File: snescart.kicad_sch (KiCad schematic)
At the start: 5 parts, among them P1 CASSETTE, U2 27C512

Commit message: fix cic
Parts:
- removed U1: ~, Package_DIP:DIP-18_W7.62mm, symbol SNES_Library:CIC
- added C3: C, Capacitor_THT:C_Disc_D4.3mm_W1.9mm_P5.00mm, symbol Device:C
- added U2: ~, Package_DIP:DIP-16_W7.62mm, symbol SNES_Library:CARTCIC
- renumbered U2 to U1
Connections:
- net GND: now also U2.4 (GND), U2.8 (GND)
- net VCC: now also U2.16 (Vcc)
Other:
- moved on the sheet: C2
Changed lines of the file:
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@@
 (kicad_sch (version 20230121) (generator eeschema)
   (paper "A4")
-  (junction (at 79.375 53.34) (diameter 0) (color 0 0 0 0)
+  (junction (at 53.34 70.485) (diameter 0) (color 0 0 0 0)
   )
   (junction (at 48.26 98.425) (diameter 0) (color 0 0 0 0)
@@
     (stroke (width 0) (type default))
   )
-  (wire (pts (xy 74.295 53.34) (xy 79.375 53.34))
-    (stroke (width 0) (type default))
-  )
   (wire (pts (xy 48.26 98.425) (xy 69.85 98.425))
     (stroke (width 0) (type default))
@@
     (stroke (width 0) (type default))
   )
-  (wire (pts (xy 79.375 53.34) (xy 85.09 53.34))
-    (stroke (width 0) (type default))
-  )
   (wire (pts (xy 80.01 121.285) (xy 113.03 121.285))
     (stroke (width 0) (type default))
@@
     (stroke (width 0) (type default))
   )
-  (symbol (lib_id "power:GND") (at 85.09 60.96 0) (unit 1)
-    (in_bom yes) (on_board yes) (dnp no) (fields_autoplaced)
-    (property "Reference" "#PWR06" (at 85.09 67.31 0)
-      (effects (font (size 1.27 1.27)) hide)
-    )
-    (property "Value" "GND" (at 85.09 66.04 0)
-      (effects (font (size 1.27 1.27)))
-    )
-    (property "Footprint" "" (at 85.09 60.96 0)
-      (effects (font (size 1.27 1.27)) hide)
-    )
-    (property "Datasheet" "" (at 85.09 60.96 0)
+  (symbol (lib_id "power:GND") (at 53.34 78.105 0) (unit 1)
+    (in_bom yes) (on_board yes) (dnp no) (fields_autoplaced)
+    (property "Reference" "#PWR06" (at 53.34 84.455 0)
+      (effects (font (size 1.27 1.27)) hide)
+    )
+    (property "Value" "GND" (at 53.34 83.185 0)
+      (effects (font (size 1.27 1.27)))
+    )
+    (property "Footprint" "" (at 53.34 78.105 0)
+      (effects (font (size 1.27 1.27)) hide)
+    )
+    (property "Datasheet" "" (at 53.34 78.105 0)
       (effects (font (size 1.27 1.27)) hide)
     )
@@
     )
   )
-  (symbol (lib_id "power:VCC") (at 79.375 53.34 0) (unit 1)
-    (in_bom yes) (on_board yes) (dnp no) (fields_autoplaced)
-    (property "Reference" "#PWR05" (at 79.375 57.15 0)
-      (effects (font (size 1.27 1.27)) hide)
-    )
-    (property "Value" "VCC" (at 79.375 49.53 0)
-      (effects (font (size 1.27 1.27)))
-    )
-    (property "Footprint" "" (at 79.375 53.34 0)
-      (effects (font (size 1.27 1.27)) hide)
-    )
-    (property "Datasheet" "" (at 79.375 53.34 0)
+  (symbol (lib_id "Device:C") (at 43.815 53.975 0) (unit 1)
+    (in_bom yes) (on_board yes) (dnp no) (fields_autoplaced)
+    (property "Reference" "C3" (at 46.99 53.34 0)
+      (effects (font (size 1.27 1.27)) (justify left))
+    )
+    (property "Value" "C" (at 46.99 55.88 0)
+      (effects (font (size 1.27 1.27)) (justify left))
+    )
+    (property "Footprint" "Capacitor_THT:C_Disc_D4.3mm_W1.9mm_P5.00mm" (at 44.7802 57.785 0)
+      (effects (font (size 1.27 1.27)) hide)
+    )
+    (property "Datasheet" "~" (at 43.815 53.975 0)
+      (effects (font (size 1.27 1.27)) hide)
+    )
+    (pin "1")
+    (pin "2")
+    (instances
+      (project "snescart"
+        (path "/066a4729-7396-4945-b543-8e17bff58a3f"
+          (reference "C3") (unit 1)
+        )
+      )
+    )
+  )
+  (symbol (lib_id "power:VCC") (at 53.34 70.485 90) (unit 1)
+    (in_bom yes) (on_board yes) (dnp no)
+    (property "Reference" "#PWR05" (at 57.15 70.485 0)
+      (effects (font (size 1.27 1.27)) hide)
+    )
+    (property "Value" "VCC" (at 46.355 70.485 90)
+      (effects (font (size 1.27 1.27)) (justify right))
+    )
+    (property "Footprint" "" (at 53.34 70.485 0)
+      (effects (font (size 1.27 1.27)) hide)
+    )
+    (property "Datasheet" "" (at 53.34 70.485 0)
       (effects (font (size 1.27 1.27)) hide)
     )
@@
     )
   )
-  (symbol (lib_id "Device:C") (at 85.09 57.15 0) (unit 1)
-    (in_bom yes) (on_board yes) (dnp no) (fields_autoplaced)
-    (property "Reference" "C2" (at 88.9 56.515 0)
+  (symbol (lib_id "Device:C") (at 53.34 74.295 0) (unit 1)
+    (in_bom yes) (on_board yes) (dnp no) (fields_autoplaced)
+    (property "Reference" "C2" (at 57.15 73.66 0)
       (effects (font (size 1.27 1.27)) (justify left))
     )
-    (property "Value" "C" (at 88.9 59.055 0)
+    (property "Value" "C" (at 57.15 76.2 0)
       (effects (font (size 1.27 1.27)) (justify left))
     )
-    (property "Footprint" "Capacitor_THT:C_Disc_D4.3mm_W1.9mm_P5.00mm" (at 86.0552 60.96 0)
-      (effects (font (size 1.27 1.27)) hide)
-    )
-    (property "Datasheet" "~" (at 85.09 57.15 0)
+    (property "Footprint" "Capacitor_THT:C_Disc_D4.3mm_W1.9mm_P5.00mm" (at 54.3052 78.105 0)
+      (effects (font (size 1.27 1.27)) hide)
+    )
+    (property "Datasheet" "~" (at 53.34 74.295 0)
       (effects (font (size 1.27 1.27)) hide)
     )
@@
   (symbol (lib_id "Memory_EPROM:27C512") (at 69.85 126.365 0) (mirror y) (unit 1)
     (in_bom yes) (on_board yes) (dnp no) (fields_autoplaced)
-    (property "Reference" "U2" (at 70.4341 96.52 0)
+    (property "Reference" "U1" (at 70.4341 96.52 0)
       (effects (font (size 1.27 1.27)) (justify right))
     )
@@
       (project "snescart"
         (path "/066a4729-7396-4945-b543-8e17bff58a3f"
-          (reference "U2") (unit 1)
+          (reference "U1") (unit 1)
         )
       )
@@
     )
   )
+  (symbol (lib_id "power:GND") (at 53.34 65.405 270) (unit 1)
+    (in_bom yes) (on_board yes) (dnp no)
+    (property "Reference" "#PWR09" (at 46.99 65.405 0)
+      (effects (font (size 1.27 1.27)) hide)
+    )
+    (property "Value" "GND" (at 46.355 65.405 90)
+      (effects (font (size 1.27 1.27)) (justify left))
+    )
+    (property "Footprint" "" (at 53.34 65.405 0)
+      (effects (font (size 1.27 1.27)) hide)
+    )
+    (property "Datasheet" "" (at 53.34 65.405 0)
+      (effects (font (size 1.27 1.27)) hide)
+    )
+    (pin "1")
+    (instances
+      (project "snescart"
+        (path "/066a4729-7396-4945-b543-8e17bff58a3f"
+          (reference "#PWR09") (unit 1)
+        )
+      )
+    )
+  )
   (symbol (lib_id "power:GND") (at 138.43 133.985 90) (unit 1)
     (in_bom yes) (on_board yes) (dnp no) (fields_autoplaced)
@@
         (path "/066a4729-7396-4945-b543-8e17bff58a3f"
           (reference "#PWR08") (unit 1)
-        )
-      )
-    )
-  )
-  (symbol (lib_id "SNES_Library:CIC") (at 66.675 62.23 0) (unit 1)
-    (in_bom yes) (on_board yes) (dnp no) (fields_autoplaced)
-    (property "Reference" "U1" (at 66.04 50.165 0)
-      (effects (font (size 1.27 1.27)))
-    )
-    (property "Value" "~" (at 61.595 48.26 0)
-      (effects (font (size 1.27 1.27)))
-    )
-    (property "Footprint" "Package_DIP:DIP-18_W7.62mm" (at 61.595 48.26 0)
-      (effects (font (size 1.27 1.27)) hide)
-    )
-    (property "Datasheet" "" (at 61.595 48.26 0)
-      (effects (font (size 1.27 1.27)) hide)
-    )
-    (pin "1")
-    (pin "10")
-    (pin "11")
-    (pin "12")
-    (pin "13")
-    (pin "14")
-    (pin "15")
-    (pin "16")
-    (pin "17")
-    (pin "18")
-    (pin "2")
-    (pin "3")
-    (pin "4")
-    (pin "5")
-    (pin "6")
-    (pin "7")
-    (pin "8")
-    (pin "9")
-    (instances
-      (project "snescart"
-        (path "/066a4729-7396-4945-b543-8e17bff58a3f"
-          (reference "U1") (unit 1)
         )
       )
@@
     )
   )
-  (symbol (lib_id "power:GND") (at 57.785 73.66 0) (unit 1)
-    (in_bom yes) (on_board yes) (dnp no) (fields_autoplaced)
-    (property "Reference" "#PWR04" (at 57.785 80.01 0)
-      (effects (font (size 1.27 1.27)) hide)
-    )
-    (property "Value" "GND" (at 57.785 78.74 0)
-      (effects (font (size 1.27 1.27)))
-    )
-    (property "Footprint" "" (at 57.785 73.66 0)
-      (effects (font (size 1.27 1.27)) hide)
-    )
-    (property "Datasheet" "" (at 57.785 73.66 0)
+  (symbol (lib_id "power:GND") (at 53.34 67.945 270) (unit 1)
+    (in_bom yes) (on_board yes) (dnp no)
+    (property "Reference" "#PWR04" (at 46.99 67.945 0)
+      (effects (font (size 1.27 1.27)) hide)
+    )
+    (property "Value" "GND" (at 46.355 67.945 90)
+      (effects (font (size 1.27 1.27)) (justify left))
+    )
+    (property "Footprint" "" (at 53.34 67.945 0)
+      (effects (font (size 1.27 1.27)) hide)
+    )
+    (property "Datasheet" "" (at 53.34 67.945 0)
       (effects (font (size 1.27 1.27)) hide)
     )
@@
         )
       )
+    )
+  )
+  (symbol (lib_id "SNES_Library:CARTCIC") (at 60.96 59.055 0) (unit 1)
+    (in_bom yes) (on_board yes) (dnp no) (fields_autoplaced)
+    (property "Reference" "U2" (at 60.96 48.26 0)
+      (effects (font (size 1.27 1.27)))
+    )
+    (property "Value" "~" (at 53.34 50.165 0)
+      (effects (font (size 1.27 1.27)))
+    )
+    (property "Footprint" "Package_DIP:DIP-16_W7.62mm" (at 53.34 50.165 0)
+      (effects (font (size 1.27 1.27)) hide)
+    )
+    (property "Datasheet" "" (at 53.34 50.165 0)
+      (effects (font (size 1.27 1.27)) hide)
+    )
+    (pin "1")
+    (pin "10")
+    (pin "11")
+    (pin "12")
+    (pin "13")
+    (pin "14")
+    (pin "15")
+    (pin "16")
+    (pin "2")
+    (pin "3")
+    (pin "4")
+    (pin "5")
+    (pin "6")
+    (pin "7")
+    (pin "8")
+    (pin "9")
+    (instances
+      (project "snescart"
+        (path "/066a4729-7396-4945-b543-8e17bff58a3f"
+          (reference "U2") (unit 1)
+        )
+      )

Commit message: feet
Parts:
- removed U1: 27C512, Package_DIP:DIP-28_W15.24mm, symbol Memory_EPROM:27C512
- added U3: 27C080, symbol Memory_EPROM:27C080
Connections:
- net GND: now also U3.16 (GND)
- net VCC: now also P1.27 (+5V), P1.58 (+5V), U3.32 (VCC)
- net at P1.17 (A0): now also U3.12 (A0)
- net at P1.19 (D0): now also U3.13 (D0)
- net at P1.20 (D1): now also U3.14 (D1)
- net at P1.21 (D2): now also U3.15 (D2)
- net at P1.22 (D3): now also U3.17 (D3)
- net at P1.7 (A10): now also U3.23 (A10)
- net at P1.6 (A11): now also U3.25 (A11)
- net at P1.8 (A9): now also U3.26 (A9)
- net at P1.9 (A8): now also U3.27 (A8)
- net at P1.10 (A7): now also U3.5 (A7)
- net at P1.11 (A6): now also U3.6 (A6)
- net at P1.12 (A5): now also U3.7 (A5)
- net at P1.13 (A4): now also U3.8 (A4)
- net at P1.14 (A3): now also U3.9 (A3)
- net at P1.15 (A2): now also U3.10 (A2)
- net at P1.16 (A1): now also U3.11 (A1)
- net at P1.24 (CIC0): now also U2.1 (pad24)
- net at P1.25 (CIC2): now also U2.2 (pad55)
- net at P1.37 (A12): now also U3.4 (A12)
- net at P1.38 (A13): now also U3.28 (A13)
- net at P1.39 (A14): now also U3.29 (A14)
- net at P1.40 (A15): now also U3.3 (A15)
- net at P1.41 (A16): now also U3.2 (A16)
- net at P1.42 (A17): now also U3.30 (A17)
- net at P1.43 (A18): now also U3.31 (A18)
- net at P1.44 (A19): now also U3.1 (A19)
- net at P1.50 (D4): now also U3.18 (D4)
- net at P1.51 (D5): now also U3.19 (D5)
- net at P1.52 (D6): now also U3.20 (D6)
- net at P1.53 (D7): now also U3.21 (D7)
- net at P1.55 (CIC1): now also U2.7 (pad25)
- net at P1.56 (CIC3): now also U2.6 (pad56)
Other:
- moved on the sheet: C2, C3, U2

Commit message: edge
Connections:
- net GND: now also P1.SHIELD (GND)
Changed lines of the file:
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@@
+    )
+  )
+  (symbol (lib_id "power:GND") (at 113.03 62.865 270) (unit 1)
+    (in_bom yes) (on_board yes) (dnp no) (fields_autoplaced)
+    (property "Reference" "#PWR012" (at 106.68 62.865 0)
+      (effects (font (size 1.27 1.27)) hide)
+    )
+    (property "Value" "GND" (at 109.22 63.5 90)
+      (effects (font (size 1.27 1.27)) (justify right))
+    )
+    (property "Footprint" "" (at 113.03 62.865 0)
+      (effects (font (size 1.27 1.27)) hide)
+    )
+    (property "Datasheet" "" (at 113.03 62.865 0)
+      (effects (font (size 1.27 1.27)) hide)
+    )
+    (pin "1")
+    (instances
+      (project "snescart"
+        (path "/066a4729-7396-4945-b543-8e17bff58a3f"
+          (reference "#PWR012") (unit 1)
+        )
+      )
     )
   )
@@
         )
       )
+    )
+  )
+  (symbol (lib_id "power:GND") (at 138.43 62.865 90) (unit 1)
+    (in_bom yes) (on_board yes) (dnp no) (fields_autoplaced)
+    (property "Reference" "#PWR013" (at 144.78 62.865 0)
+      (effects (font (size 1.27 1.27)) hide)
+    )
+    (property "Value" "GND" (at 142.4171 63.5 90)
+      (effects (font (size 1.27 1.27)) (justify right))
+    )
+    (property "Footprint" "" (at 138.43 62.865 0)
+      (effects (font (size 1.27 1.27)) hide)
+    )
+    (property "Datasheet" "" (at 138.43 62.865 0)
+      (effects (font (size 1.27 1.27)) hide)
+    )
+    (pin "1")
+    (instances
+      (project "snescart"
+        (path "/066a4729-7396-4945-b543-8e17bff58a3f"
+          (reference "#PWR013") (unit 1)
+        )
+      )

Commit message: tracks
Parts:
- C3: footprint Capacitor_THT:C_Disc_D4.3mm_W1.9mm_P5.00mm -> Capacitor_THT:CP_Axial_L10.0mm_D4.5mm_P15.00mm_Horizontal
- U3: footprint (none) -> Package_DIP:DIP-32_W15.24mm
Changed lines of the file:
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@@
       (effects (font (size 1.27 1.27)) (justify left))
     )
-    (property "Footprint" "Capacitor_THT:C_Disc_D4.3mm_W1.9mm_P5.00mm" (at 113.03 23.7998 0)
+    (property "Footprint" "Capacitor_THT:CP_Axial_L10.0mm_D4.5mm_P15.00mm_Horizontal" (at 113.03 23.7998 0)
       (effects (font (size 1.27 1.27)) hide)
     )
@@
       (effects (font (size 1.27 1.27)) (justify right))
     )
-    (property "Footprint" "" (at 69.85 131.445 0)
-      (effects (font (size 1.27 1.27)) hide)
-    )
+    (property "Footprint" "Package_DIP:DIP-32_W15.24mm" (at 69.85 131.445 0)
+      (effects (font (size 1.27 1.27)) hide)
+    )

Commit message: funny cap
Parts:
- C1: footprint Capacitor_THT:C_Disc_D4.3mm_W1.9mm_P5.00mm -> Library:CapacitorSpecial
- C2: footprint Capacitor_THT:C_Disc_D4.3mm_W1.9mm_P5.00mm -> Library:Capacitor
- C3: footprint Capacitor_THT:CP_Axial_L10.0mm_D4.5mm_P15.00mm_Horizontal -> Library:Capacitor
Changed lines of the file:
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@@
       (effects (font (size 1.27 1.27)))
     )
-    (property "Footprint" "Capacitor_THT:C_Disc_D4.3mm_W1.9mm_P5.00mm" (at 48.26 97.4598 0)
+    (property "Footprint" "Library:CapacitorSpecial" (at 48.26 97.4598 0)
       (effects (font (size 1.27 1.27)) hide)
     )
@@
       (effects (font (size 1.27 1.27)) (justify left))
     )
-    (property "Footprint" "Capacitor_THT:CP_Axial_L10.0mm_D4.5mm_P15.00mm_Horizontal" (at 113.03 23.7998 0)
+    (property "Footprint" "Library:Capacitor" (at 113.03 23.7998 0)
       (effects (font (size 1.27 1.27)) hide)
     )
@@
       (effects (font (size 1.27 1.27)) (justify left))
     )
-    (property "Footprint" "Capacitor_THT:C_Disc_D4.3mm_W1.9mm_P5.00mm" (at 150.495 30.7848 0)
+    (property "Footprint" "Library:Capacitor" (at 150.495 30.7848 0)
       (effects (font (size 1.27 1.27)) hide)
     )

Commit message: date
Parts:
- renumbered U3 to U1
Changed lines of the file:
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@@
   (symbol (lib_id "Memory_EPROM:27C080") (at 69.85 131.445 0) (mirror y) (unit 1)
     (in_bom yes) (on_board yes) (dnp no) (fields_autoplaced)
-    (property "Reference" "U3" (at 70.4341 96.52 0)
+    (property "Reference" "U1" (at 70.4341 96.52 0)
       (effects (font (size 1.27 1.27)) (justify right))
     )
@@
       (project "snescart"
         (path "/066a4729-7396-4945-b543-8e17bff58a3f"
-          (reference "U3") (unit 1)
+          (reference "U1") (unit 1)
         )
       )

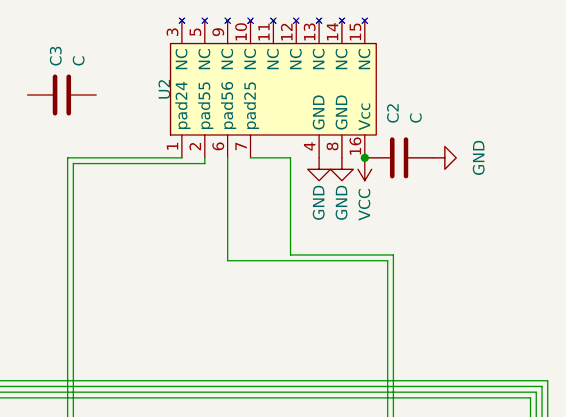
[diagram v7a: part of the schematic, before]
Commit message: bottom vcc
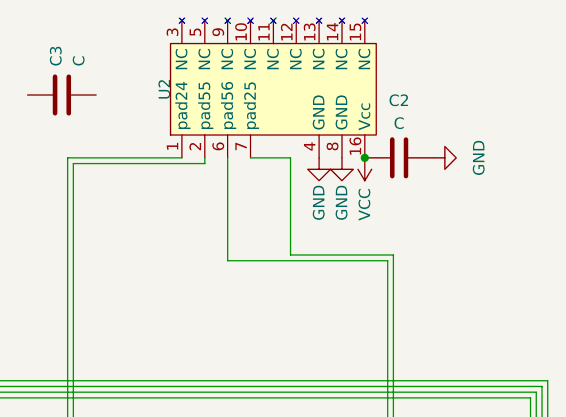
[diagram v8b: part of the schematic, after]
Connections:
- net GND: now also C2.1; no longer C2.2
- net VCC: now also C2.2; no longer C2.1
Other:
- moved on the sheet: C2
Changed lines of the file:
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@@
     )
   )
-  (symbol (lib_id "Device:C") (at 146.685 31.75 90) (unit 1)
+  (symbol (lib_id "Device:C") (at 146.685 31.75 270) (unit 1)
     (in_bom yes) (on_board yes) (dnp no) (fields_autoplaced)
-    (property "Reference" "C2" (at 146.05 27.94 0)
-      (effects (font (size 1.27 1.27)) (justify left))
+    (property "Reference" "C2" (at 146.685 25.4 90)
+      (effects (font (size 1.27 1.27)))
     )
-    (property "Value" "C" (at 148.59 27.94 0)
-      (effects (font (size 1.27 1.27)) (justify left))
+    (property "Value" "C" (at 146.685 27.94 90)
+      (effects (font (size 1.27 1.27)))
     )
-    (property "Footprint" "Library:Capacitor" (at 150.495 30.7848 0)
+    (property "Footprint" "Library:Capacitor" (at 142.875 32.7152 0)
       (effects (font (size 1.27 1.27)) hide)
     )
